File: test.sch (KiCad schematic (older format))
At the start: 208 parts, among them J1 HSP2_MX-502584-0670, J2 HSP2_MX-502584-0670, J3 HSP2_MX-502584-0670, J4 HSP2_MX-502584-0670, J5 HSP2_MX-502584-0670, J6 HSP2_MX-502584-0670, J7 CONN_02X01, J8 CONN_02X01, J9 microSD, P1 Gniazdo akumulatora, P2 Gniazdo akumulatora, P3 Gniazdo programatora SWD, T1 IRLML6401, T10 BSS138, T11 BSS138, T12 BSS138, T13 BSS138, T14 FDV304P, T2 IRLML6401, T3 IRLML6401, T4 IRLML6401, T5 IRLML6401, T6 IRLML6401, T7 BSS138, T8 BSS138, T9 BSS138, U1 MCP1755T-3302E/DC, U10 TPS3823, U11 STM32L051R8, U12 DS3231SN, U13 MCP1755T-3302E/DC, U14 MCP1755T-3302E/DC, U15 MIC29302, U16 DHT22, U17 M590E, U18 S25FL1275ABMGI101, U19 ESP-07, U2 MCP1755T-3302E/DC, U20 SIMHOLDER, U3 MCP1755T-3302E/DC, U4 MCP1755T-3302E/DC, U5 MCP1755T-3302E/DC, U6 MCP1755T-3302E/DC, U7 74LVX373M, U8 74LVX373M, U9 MAX3485, Y1 32.768 kHz, Y2 8 MHz

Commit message: łączenie ścieżek pcb
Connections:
- wire segments 665 -> 667
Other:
- moved on the sheet: C32, F10, F9

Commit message: rutowanie pcb
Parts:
- removed R51: 1k, Resistors_SMD:R_0603, symbol R
- removed TP1, TP2, TP3, TP4, TP5, TP6: TEST, Measurement_Points:Measurement_Point_Round-SMD-Pad_Big, symbol TEST
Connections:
- wire segments 667 -> 660
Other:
- moved on the sheet: BT1, C38, C43, C47, C49, F11, R40, R42, R44, TP22

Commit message: sprawdzanie drc pcb
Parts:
- removed TP19, TP20: TEST, Measurement_Points:Measurement_Point_Round-SMD-Pad_Big, symbol TEST
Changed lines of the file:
@@
 $EndComp
 $Comp
-L TEST TP19
-U 1 1 5944C9E1
-P 9625 9350
-F 0 "TP19" H 9625 9650 50  0000 C BNN
-F 1 "TEST" H 9625 9600 50  0000 C CNN
-F 2 "Measurement_Points:Measurement_Point_Round-SMD-Pad_Big" H 9625 9350 50  0001 C CNN
-F 3 "" H 9625 9350 50  0001 C CNN
-	1    9625 9350
-	1    0    0    -1
-$EndComp
-$Comp
 L TEST TP21
 U 1 1 5944F03D
@@
 $EndComp
 $Comp
-L TEST TP20
-U 1 1 597D63D3
-P 9625 10450
-F 0 "TP20" H 9625 10750 50  0000 C BNN
-F 1 "TEST" H 9625 10700 50  0000 C CNN
-F 2 "Measurement_Points:Measurement_Point_Round-SMD-Pad_Big" H 9625 10450 50  0001 C CNN
-F 3 "" H 9625 10450 50  0001 C CNN
-	1    9625 10450
-	1    0    0    -1
-$EndComp
-$Comp
 L CP C47
 U 1 1 5980A533
@@
 Connection ~ 6375 9175
 Wire Wire Line
-	9625 9350 9625 9400
-Connection ~ 9625 9400
-Wire Wire Line
 	10425 5900 10425 5950
 Wire Wire Line
@@
 	10550 10450 10550 10500
 Connection ~ 10550 10500
-Wire Wire Line
-	9625 10450 9625 10500
-Connection ~ 9625 10500
 Wire Notes Line
 	13100 8075 13100 8600

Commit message: przesunięcie karty sim i cr2032
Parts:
- U11: footprint Housings_QFP:LQFP-64_10x10mm_Pitch0.5mm -> footprints:LQFP-64_10x10mm_Pitch0.5mm
- U18: footprint Power_Integrations:SO-8 -> footprints:SO-8
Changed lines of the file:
@@
 F 0 "U18" H 13950 6700 60  0000 C CNN
 F 1 "S25FL1275ABMGI101" H 13975 6275 60  0000 C CNN
-F 2 "Power_Integrations:SO-8" H 13900 6525 60  0001 C CNN
+F 2 "footprints:SO-8" H 13900 6525 60  0001 C CNN
 F 3 "" H 13900 6525 60  0001 C CNN
 	1    13950 6350
@@
 F 0 "U11" H 8475 5050 60  0000 C CNN
 F 1 "STM32L051R8" H 8475 4950 60  0000 C CNN
-F 2 "Housings_QFP:LQFP-64_10x10mm_Pitch0.5mm" H 8075 4600 60  0001 C CNN
+F 2 "footprints:LQFP-64_10x10mm_Pitch0.5mm" H 8075 4600 60  0001 C CNN
 F 3 "" H 8075 4600 60  0001 C CNN
 	1    7925 4450

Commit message: img
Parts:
- added R? (x2): 1k, Resistors_SMD:R_0603, symbol R
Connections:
- net GSM_DTR: now also R?.2; no longer U17.9 (DTR)
- net GSM_ON: now also R?.2; no longer U17.19 (ON/OFF)
- new net: R?.1, U17.19 (ON/OFF)
- new net: R?.1, U17.9 (DTR)
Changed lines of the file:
@@
 	10825 3000 11325 3000
 Wire Wire Line
-	10675 2850 13300 2850
-Wire Wire Line
 	10750 2925 12675 2925
-Wire Wire Line
-	14400 3850 9400 3850
 Wire Wire Line
 	8975 5200 8975 4800
@@
 	1    0    0    -1
 $EndComp
+$Comp
+L R R?
+U 1 1 5980C966
+P 12825 3850
+F 0 "R?" V 12905 3850 50  0000 C CNN
+F 1 "1k" V 12825 3850 50  0000 C CNN
+F 2 "Resistors_SMD:R_0603" V 12755 3850 50  0001 C CNN
+F 3 "" H 12825 3850 50  0000 C CNN
+	1    12825 3850
+	0    1    1    0
+$EndComp
+$Comp
+L R R?
+U 1 1 5980CC56
+P 11475 2850
+F 0 "R?" V 11375 2850 50  0000 C CNN
+F 1 "1k" V 11475 2850 50  0000 C CNN
+F 2 "Resistors_SMD:R_0603" V 11405 2850 50  0001 C CNN
+F 3 "" H 11475 2850 50  0000 C CNN
+	1    11475 2850
+	0    1    1    0
+$EndComp
+Wire Wire Line
+	14400 3850 12975 3850
+Wire Wire Line
+	12675 3850 9400 3850
+Wire Wire Line
+	11625 2850 13300 2850
+Wire Wire Line
+	10675 2850 11325 2850
 $EndSCHEMATC

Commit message: cap 3d skala +2xGSM rez
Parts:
- gave numbers to parts that had none: 2
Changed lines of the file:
@@
 $EndComp
 $Comp
-L R R?
+L R R60
 U 1 1 5980C966
 P 12825 3850
-F 0 "R?" V 12905 3850 50  0000 C CNN
+F 0 "R60" V 12905 3850 50  0000 C CNN
 F 1 "1k" V 12825 3850 50  0000 C CNN
 F 2 "Resistors_SMD:R_0603" V 12755 3850 50  0001 C CNN
@@
 $EndComp
 $Comp
-L R R?
+L R R51
 U 1 1 5980CC56
 P 11475 2850
-F 0 "R?" V 11375 2850 50  0000 C CNN
+F 0 "R51" V 11375 2850 50  0000 C CNN
 F 1 "1k" V 11475 2850 50  0000 C CNN
 F 2 "Resistors_SMD:R_0603" V 11405 2850 50  0001 C CNN

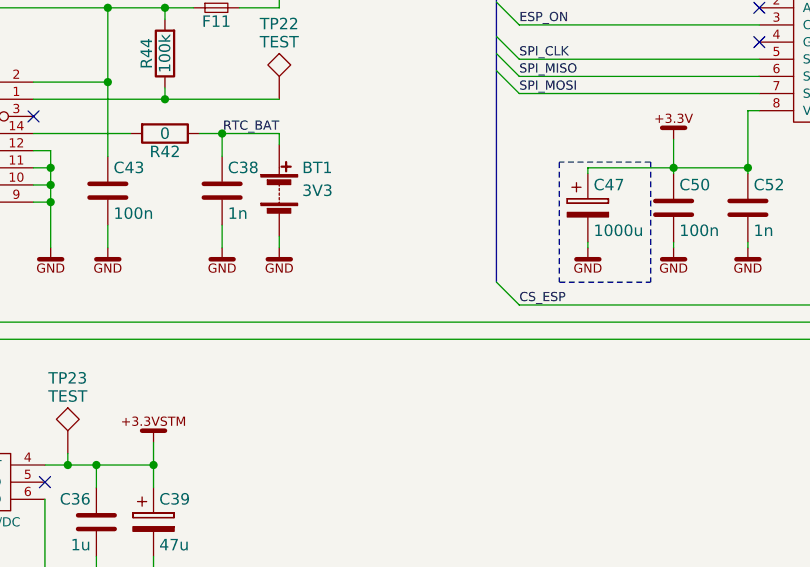
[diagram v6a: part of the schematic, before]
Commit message: +tp1 tp2 zmieniono strefy miedzi
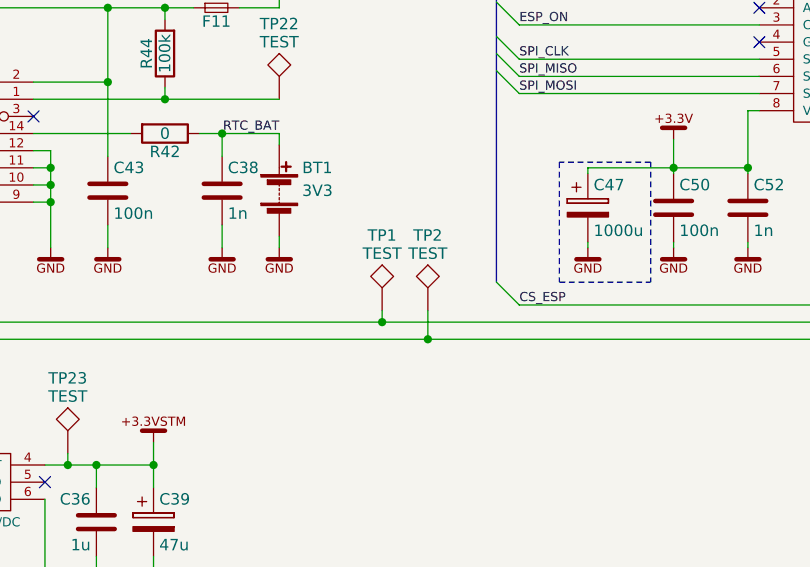
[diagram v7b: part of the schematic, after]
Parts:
- added TP1, TP2: TEST, Measurement_Points:Measurement_Point_Round-SMD-Pad_Big, symbol TEST
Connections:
- net URT2_RX: now also TP1.1
- net URT2_TX: now also TP2.1

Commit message: ustalanie kosztorysu
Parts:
- renumbered P3 to J10, P1 to J11, P2 to J12, U20 to J13
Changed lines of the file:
@@
 VBAT OPT. 3.9V
 $Comp
-L SIMHOLDER U20
+L SIMHOLDER J13
 U 1 1 58BE6757
 P 15175 2800
-F 0 "U20" H 15175 3000 60  0000 C CNN
+F 0 "J13" H 15175 3000 60  0000 C CNN
 F 1 "SIMHOLDER" H 15200 2650 60  0000 C CNN
 F 2 "footprints:AMPHENOL_SIMHOLDER_C707_10M006_049_2" H 15125 2825 60  0001 C CNN
@@
 $EndComp
 $Comp
-L CONN_01X04 P3
+L CONN_01X04 J10
 U 1 1 592FF26E
 P 9650 925
-F 0 "P3" H 9650 1175 50  0000 C CNN
+F 0 "J10" H 9650 1175 50  0000 C CNN
 F 1 "Gniazdo programatora SWD" V 9750 925 50  0000 C CNN
 F 2 "footprints:MX-502584-0470" H 9650 925 50  0001 C CNN
@@
 $EndComp
 $Comp
-L CONN_01X04 P1
+L CONN_01X04 J11
 U 1 1 5930E54A
 P 5375 9325
-F 0 "P1" H 5375 9575 50  0000 C CNN
+F 0 "J11" H 5375 9575 50  0000 C CNN
 F 1 "Gniazdo akumulatora" V 5475 9325 50  0000 C CNN
 F 2 "footprints:MX-171813-0004" H 5375 9325 50  0001 C CNN
@@
 $EndComp
 $Comp
-L CONN_01X04 P2
+L CONN_01X04 J12
 U 1 1 593ACE9B
 P 5375 10475
-F 0 "P2" H 5375 10725 50  0000 C CNN
+F 0 "J12" H 5375 10725 50  0000 C CNN
 F 1 "Gniazdo akumulatora" V 5475 10475 50  0000 C CNN
 F 2 "footprints:MX-171813-0004" H 5375 10475 50  0001 C CNN
